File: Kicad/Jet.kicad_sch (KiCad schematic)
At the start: 17 parts, among them J1 Conn_02x13_Odd_Even, J2 Conn_01x03_Female, J3 POWER, J4 Conn_02x10_Odd_Even, J5 Conn_02x10_Odd_Even, Q1 Q_NPN_EBC, Q2 Q_NPN_EBC, U1 PC817, U2 PC817

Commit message: UPDATE: footprint
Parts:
- D1, D3: value D_Zener -> (none); footprint Diode_THT:D_DO-35_SOD27_P7.62mm_Horizontal -> (none)
- D2, D4: value 1N4448 -> (none); footprint Diode_THT:D_DO-35_SOD27_P7.62mm_Horizontal -> (none)
- J1: value Conn_02x13_Odd_Even -> (none); footprint IDC-Header_2x13-1MP_P2.54mm_Latch_Horizontal -> (none)
- J2: value Conn_01x03_Female -> (none); footprint Connector_PinSocket_2.54mm:PinSocket_1x03_P2.54mm_Vertical -> (none)
- J3: value POWER -> (none); footprint Connector_PinSocket_2.54mm:PinSocket_1x02_P2.54mm_Vertical -> (none)
- J4, J5: value Conn_02x10_Odd_Even -> (none); footprint IDC-Header_2x10-1MP_P2.54mm_Latch_Vertical -> (none)
- Q1, Q2: value Q_NPN_EBC -> (none); footprint TO-92L_HandSolder -> (none)
- R1, R2, R3, R4: value R -> (none); footprint Resistor_SMD:R_0805_2012Metric_Pad1.20x1.40mm_HandSolder -> (none)
- U1, U2: value PC817 -> (none); footprint Package_DIP:DIP-4_W7.62mm -> (none)

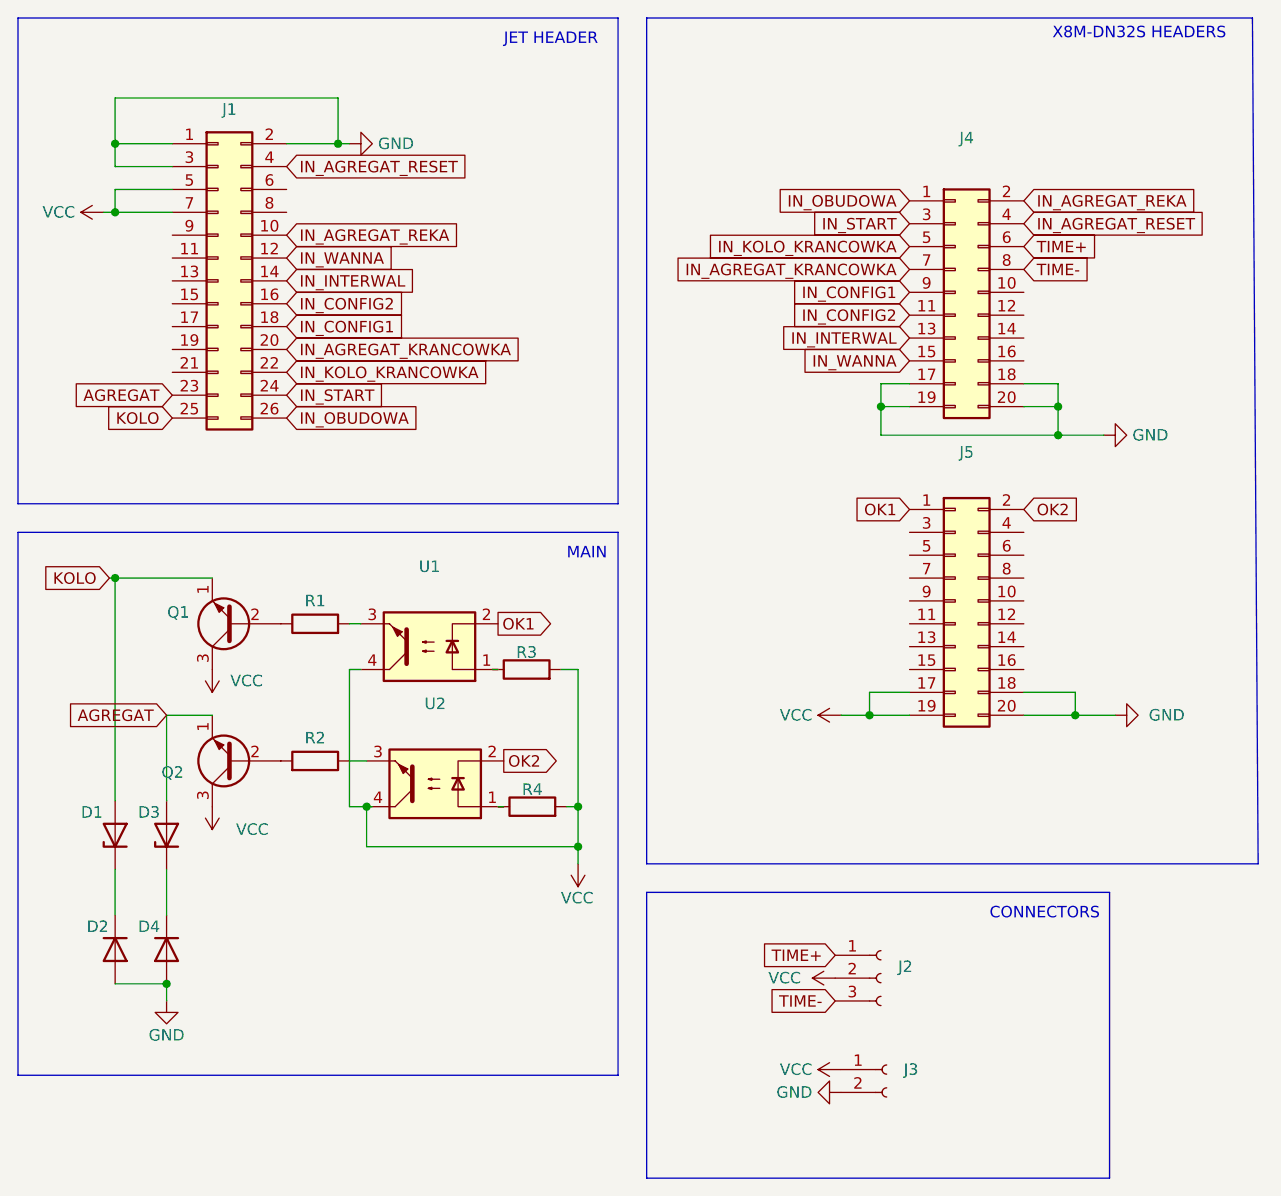
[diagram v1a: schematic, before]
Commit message: FIX Transistor footprin
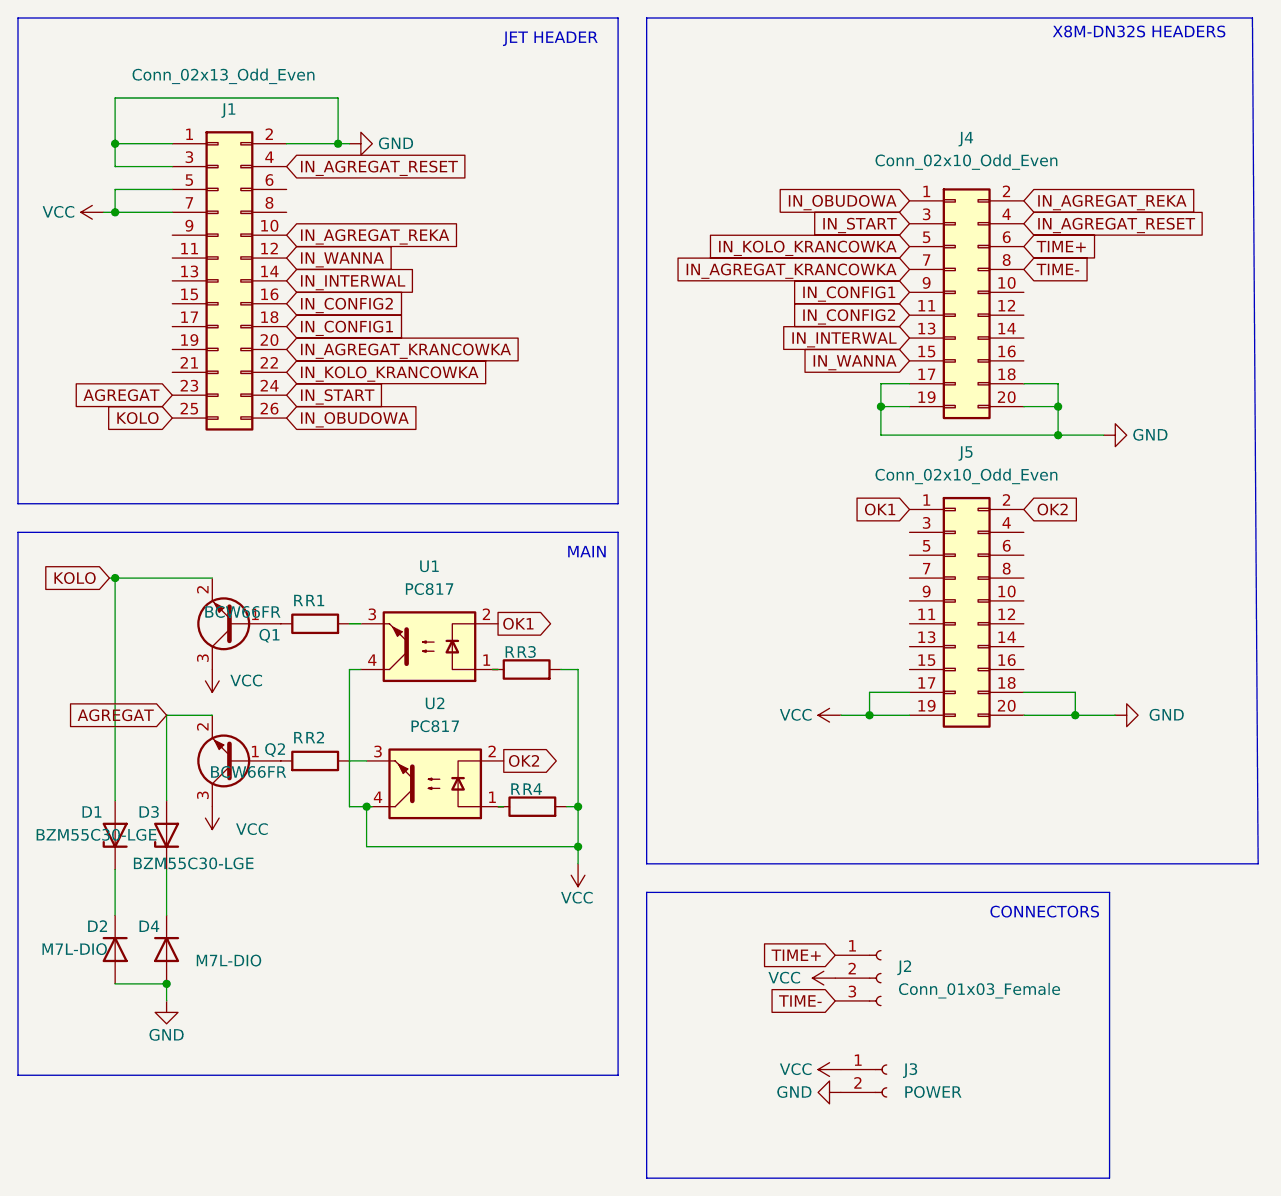
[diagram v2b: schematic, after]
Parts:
- D1, D3: value (none) -> BZM55C30-LGE; footprint (none) -> D_MiniMELF
- D2, D4: value (none) -> M7L-DIO; footprint (none) -> Diode_SMD:D_SMA
- J1: value (none) -> Conn_02x13_Odd_Even; footprint (none) -> IDC-Header_2x13-1MP_P2.54mm_Latch_Horizontal
- J2: value (none) -> Conn_01x03_Female; footprint (none) -> Connector_PinSocket_2.54mm:PinSocket_1x03_P2.54mm_Vertical
- J3: value (none) -> POWER; footprint (none) -> Connector_PinSocket_2.54mm:PinSocket_1x02_P2.54mm_Vertical
- J4, J5: value (none) -> Conn_02x10_Odd_Even; footprint (none) -> IDC-Header_2x10-1MP_P2.54mm_Latch_Vertical
- Q1, Q2: value (none) -> BCW66FR; footprint (none) -> Package_TO_SOT_SMD:SOT-23
- R1, R2, R3, R4: value (none) -> R; footprint (none) -> Resistor_SMD:R_0805_2012Metric_Pad1.20x1.40mm_HandSolder
- U1, U2: value (none) -> PC817; footprint (none) -> Package_DIP:DIP-4_W7.62mm
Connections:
- net AGREGAT: now also Q2.2 (E); no longer Q2.1 (E)
- net KOLO: now also Q1.2 (E); no longer Q1.1 (E)
- net at R1.1: now also Q1.1 (B); no longer Q1.2 (B)
- net at R2.2: now also Q2.1 (B); no longer Q2.2 (B)
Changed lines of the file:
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@@
     (in_bom yes) (on_board yes) (fields_autoplaced)
     (property "Reference" "U1" (id 0) (at 66.04 78.105 0))
-    (property "Value" "" (id 1) (at 66.04 80.645 0))
-    (property "Footprint" "" (id 2) (at 71.12 81.915 0)
+    (property "Value" "PC817" (id 1) (at 66.04 80.645 0))
+    (property "Footprint" "Package_DIP:DIP-4_W7.62mm" (id 2) (at 71.12 81.915 0)
       (effects (font (size 1.27 1.27) italic) (justify left) hide)
     )
@@
     (in_bom yes) (on_board yes)
     (property "Reference" "R3" (id 0) (at 76.835 87.63 90))
-    (property "Value" "" (id 1) (at 74.93 87.63 90))
-    (property "Footprint" "" (id 2) (at 76.835 91.313 90)
+    (property "Value" "R" (id 1) (at 74.93 87.63 90))
+    (property "Footprint" "Resistor_SMD:R_0805_2012Metric_Pad1.20x1.40mm_HandSolder" (id 2) (at 76.835 91.313 90)
       (effects (font (size 1.27 1.27)) hide)
     )
@@
     (in_bom yes) (on_board yes) (fields_autoplaced)
     (property "Reference" "J4" (id 0) (at 125.73 30.48 0))
-    (property "Value" "" (id 1) (at 125.73 33.02 0))
-    (property "Footprint" "" (id 2) (at 124.46 47.625 0)
+    (property "Value" "Conn_02x10_Odd_Even" (id 1) (at 125.73 33.02 0))
+    (property "Footprint" "IDC-Header_2x10-1MP_P2.54mm_Latch_Vertical" (id 2) (at 124.46 47.625 0)
       (effects (font (size 1.27 1.27)) hide)
     )
@@
       (effects (font (size 1.27 1.27)) (justify left))
     )
-    (property "Value" "" (id 1) (at 118.745 136.5249 0)
-      (effects (font (size 1.27 1.27)) (justify left))
-    )
-    (property "Footprint" "" (id 2) (at 116.84 133.985 0)
+    (property "Value" "POWER" (id 1) (at 118.745 136.5249 0)
+      (effects (font (size 1.27 1.27)) (justify left))
+    )
+    (property "Footprint" "Connector_PinSocket_2.54mm:PinSocket_1x02_P2.54mm_Vertical" (id 2) (at 116.84 133.985 0)
       (effects (font (size 1.27 1.27)) hide)
     )
@@
     (pin "1")
   )
-  (symbol (lib_id "Device:Q_NPN_EBC") (at 44.45 84.455 180) (unit 1)
-    (in_bom yes) (on_board yes) (fields_autoplaced)
-    (property "Reference" "Q1" (id 0) (at 39.37 83.1849 0)
-      (effects (font (size 1.27 1.27)) (justify left))
-    )
-    (property "Value" "" (id 1) (at 39.37 85.7249 0)
-      (effects (font (size 1.27 1.27)) (justify left))
-    )
-    (property "Footprint" "" (id 2) (at 39.37 86.995 0)
+  (symbol (lib_name "Q_NPN_EBC_1") (lib_id "Device:Q_NPN_EBC") (at 44.45 84.455 180) (unit 1)
+    (in_bom yes) (on_board yes) (fields_autoplaced)
+    (property "Reference" "Q1" (id 0) (at 49.53 85.7251 0)
+      (effects (font (size 1.27 1.27)) (justify left))
+    )
+    (property "Value" "BCW66FR" (id 1) (at 49.53 83.1851 0)
+      (effects (font (size 1.27 1.27)) (justify left))
+    )
+    (property "Footprint" "Package_TO_SOT_SMD:SOT-23" (id 2) (at 49.53 81.915 0)
       (effects (font (size 1.27 1.27)) hide)
     )
@@
     (in_bom yes) (on_board yes)
     (property "Reference" "R4" (id 0) (at 77.47 102.87 90))
-    (property "Value" "" (id 1) (at 75.565 102.87 90))
-    (property "Footprint" "" (id 2) (at 77.47 106.553 90)
+    (property "Value" "R" (id 1) (at 75.565 102.87 90))
+    (property "Footprint" "Resistor_SMD:R_0805_2012Metric_Pad1.20x1.40mm_HandSolder" (id 2) (at 77.47 106.553 90)
       (effects (font (size 1.27 1.27)) hide)
     )
@@
     (in_bom yes) (on_board yes)
     (property "Reference" "R1" (id 0) (at 53.34 81.915 90))
-    (property "Value" "" (id 1) (at 51.435 81.915 90))
-    (property "Footprint" "" (id 2) (at 53.34 86.233 90)
+    (property "Value" "R" (id 1) (at 51.435 81.915 90))
+    (property "Footprint" "Resistor_SMD:R_0805_2012Metric_Pad1.20x1.40mm_HandSolder" (id 2) (at 53.34 86.233 90)
       (effects (font (size 1.27 1.27)) hide)
     )
@@
     (in_bom yes) (on_board yes)
     (property "Reference" "J1" (id 0) (at 43.815 27.305 0))
-    (property "Value" "" (id 1) (at 43.18 23.495 0))
-    (property "Footprint" "" (id 2) (at 42.545 46.355 0)
+    (property "Value" "Conn_02x13_Odd_Even" (id 1) (at 43.18 23.495 0))
+    (property "Footprint" "IDC-Header_2x13-1MP_P2.54mm_Latch_Horizontal" (id 2) (at 42.545 46.355 0)
       (effects (font (size 1.27 1.27)) hide)
     )
@@
   (symbol (lib_id "Device:Q_NPN_EBC") (at 44.45 99.695 180) (unit 1)
     (in_bom yes) (on_board yes) (fields_autoplaced)
-    (property "Reference" "Q2" (id 0) (at 38.735 100.9651 0)
-      (effects (font (size 1.27 1.27)) (justify left))
-    )
-    (property "Value" "" (id 1) (at 38.735 98.4251 0)
-      (effects (font (size 1.27 1.27)) (justify left))
-    )
-    (property "Footprint" "" (id 2) (at 39.37 102.235 0)
+    (property "Reference" "Q2" (id 0) (at 50.165 98.4249 0)
+      (effects (font (size 1.27 1.27)) (justify left))
+    )
+    (property "Value" "BCW66FR" (id 1) (at 50.165 100.9649 0)
+      (effects (font (size 1.27 1.27)) (justify left))
+    )
+    (property "Footprint" "Package_TO_SOT_SMD:SOT-23" (id 2) (at 49.53 97.155 0)
       (effects (font (size 1.27 1.27)) hide)
     )
@@
       (effects (font (size 1.27 1.27)) hide)
     )
-    (pin "1")
-    (pin "2")
+    (pin "2")
+    (pin "1")
     (pin "3")
   )
@@
       (effects (font (size 1.27 1.27)) (justify left))
     )
-    (property "Value" "" (id 1) (at 22.86 120.65 90)
-      (effects (font (size 1.27 1.27)) (justify left))
-    )
-    (property "Footprint" "" (id 2) (at 26.67 120.65 0)
+    (property "Value" "M7L-DIO" (id 1) (at 22.86 120.65 90)
+      (effects (font (size 1.27 1.27)) (justify left))
+    )
+    (property "Footprint" "Diode_SMD:D_SMA" (id 2) (at 26.67 120.65 0)
       (effects (font (size 1.27 1.27)) hide)
     )
@@
     (in_bom yes) (on_board yes) (fields_autoplaced)
     (property "Reference" "U2" (id 0) (at 66.675 93.345 0))
-    (property "Value" "" (id 1) (at 66.675 95.885 0))
-    (property "Footprint" "" (id 2) (at 71.755 97.155 0)
+    (property "Value" "PC817" (id 1) (at 66.675 95.885 0))
+    (property "Footprint" "Package_DIP:DIP-4_W7.62mm" (id 2) (at 71.755 97.155 0)
       (effects (font (size 1.27 1.27) italic) (justify left) hide)
     )
@@
       (effects (font (size 1.27 1.27)) (justify left))
     )
-    (property "Value" "" (id 1) (at 118.11 125.0949 0)
-      (effects (font (size 1.27 1.27)) (justify left))
-    )
-    (property "Footprint" "" (id 2) (at 116.205 123.825 0)
+    (property "Value" "Conn_01x03_Female" (id 1) (at 118.11 125.0949 0)
+      (effects (font (size 1.27 1.27)) (justify left))
+    )
+    (property "Footprint" "Connector_PinSocket_2.54mm:PinSocket_1x03_P2.54mm_Vertical" (id 2) (at 116.205 123.825 0)
       (effects (font (size 1.27 1.27)) hide)
     )
@@
       (effects (font (size 1.27 1.27)) (justify right))
     )
-    (property "Value" "" (id 1) (at 33.02 111.125 90)
-      (effects (font (size 1.27 1.27)) (justify right))
-    )
-    (property "Footprint" "" (id 2) (at 36.83 107.95 0)
+    (property "Value" "BZM55C30-LGE" (id 1) (at 33.02 111.125 90)
+      (effects (font (size 1.27 1.27)) (justify right))
+    )
+    (property "Footprint" "D_MiniMELF" (id 2) (at 36.83 107.95 0)
       (effects (font (size 1.27 1.27)) hide)
     )
@@
       (effects (font (size 1.27 1.27)) (justify right))
     )
-    (property "Value" "" (id 1) (at 22.225 107.95 90)
-      (effects (font (size 1.27 1.27)) (justify right))
-    )
-    (property "Footprint" "" (id 2) (at 31.115 107.95 0)
+    (property "Value" "BZM55C30-LGE" (id 1) (at 22.225 107.95 90)
+      (effects (font (size 1.27 1.27)) (justify right))
+    )
+    (property "Footprint" "D_MiniMELF" (id 2) (at 31.115 107.95 0)
       (effects (font (size 1.27 1.27)) hide)
     )
@@
     (in_bom yes) (on_board yes) (fields_autoplaced)
     (property "Reference" "J5" (id 0) (at 125.73 65.405 0))
-    (property "Value" "" (id 1) (at 125.73 67.945 0))
-    (property "Footprint" "" (id 2) (at 124.46 81.915 0)
+    (property "Value" "Conn_02x10_Odd_Even" (id 1) (at 125.73 67.945 0))
+    (property "Footprint" "IDC-Header_2x10-1MP_P2.54mm_Latch_Vertical" (id 2) (at 124.46 81.915 0)
       (effects (font (size 1.27 1.27)) hide)
     )
@@
       (effects (font (size 1.27 1.27)) (justify right))
     )
-    (property "Value" "" (id 1) (at 40.005 121.9199 90)
-      (effects (font (size 1.27 1.27)) (justify right))
-    )
-    (property "Footprint" "" (id 2) (at 41.275 120.65 0)
+    (property "Value" "M7L-DIO" (id 1) (at 40.005 121.9199 90)
+      (effects (font (size 1.27 1.27)) (justify right))
+    )
+    (property "Footprint" "Diode_SMD:D_SMA" (id 2) (at 41.275 120.65 0)
       (effects (font (size 1.27 1.27)) hide)
     )
@@
     (in_bom yes) (on_board yes)
     (property "Reference" "R2" (id 0) (at 53.34 97.155 90))
-    (property "Value" "" (id 1) (at 51.435 97.155 90))
-    (property "Footprint" "" (id 2) (at 53.34 101.473 90)
-      (effects (font (size 1.27 1.27)) hide)
-    )
+    (property "Value" "R" (id 1) (at 51.435 97.155 90))
+    (property "Footprint" "Resistor_SMD:R_0805_2012Metric_Pad1.20x1.40mm_HandSolder" (id 2) (at 53.34 101.473 90)
+      (effects (font (size 1.27 1.27)) hide)
+    )
